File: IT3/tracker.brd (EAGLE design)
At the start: 120 x 89.3 mm, 91 parts, among them J1 THING_PLUS_PHYSICAL, Q1 2N3906, Q2 DMG6602SVT, Q3 DMG6602SVT, Q6 MMBT3906LT1SMD, Q7 DMG6602SVT, U1 ADXL343BCCZ-RL7, U2 FONA-800-BREAKOUTNOHOLE, U3 MP2155GQ-Z, U4 SPARKFUN-SWARM-M138NOTOPHOLE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

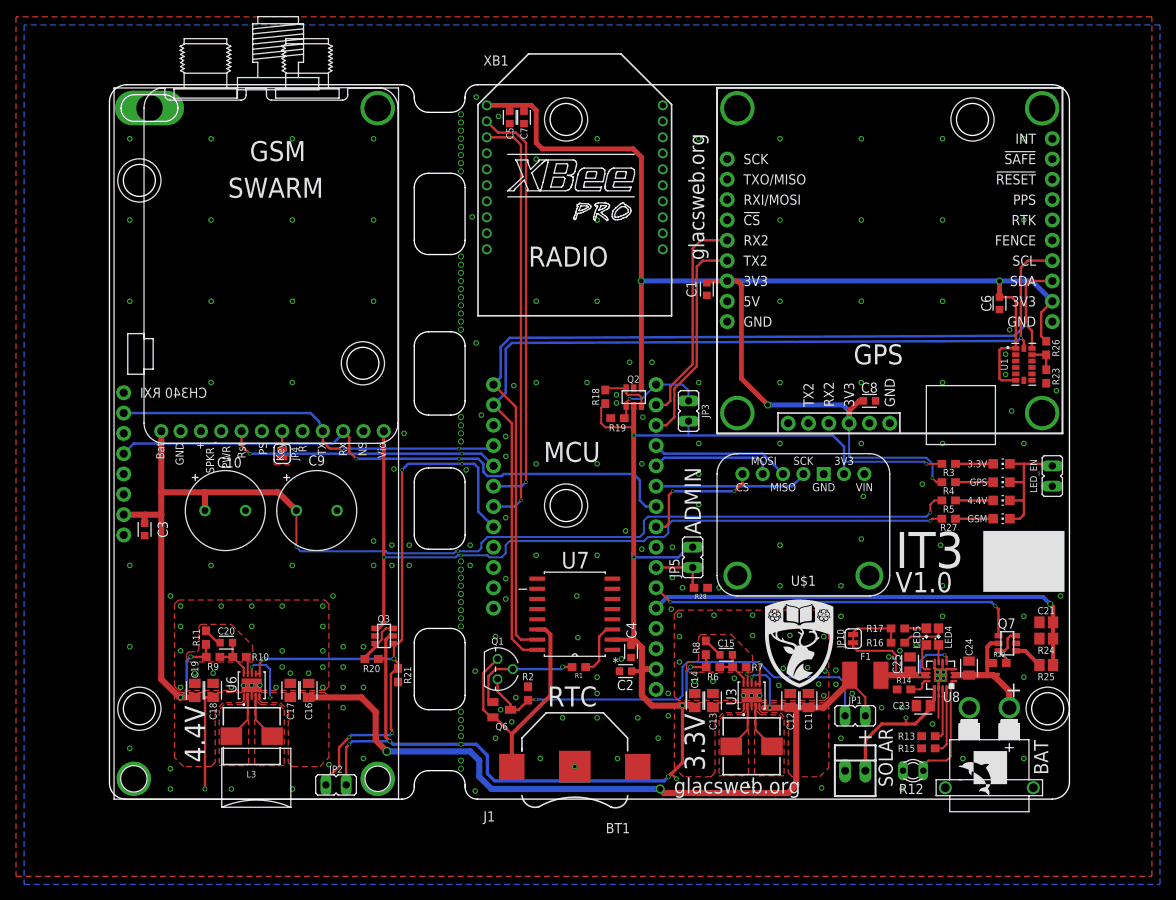
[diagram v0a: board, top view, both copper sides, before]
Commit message: Final silkscreen tweaks and generation of production files
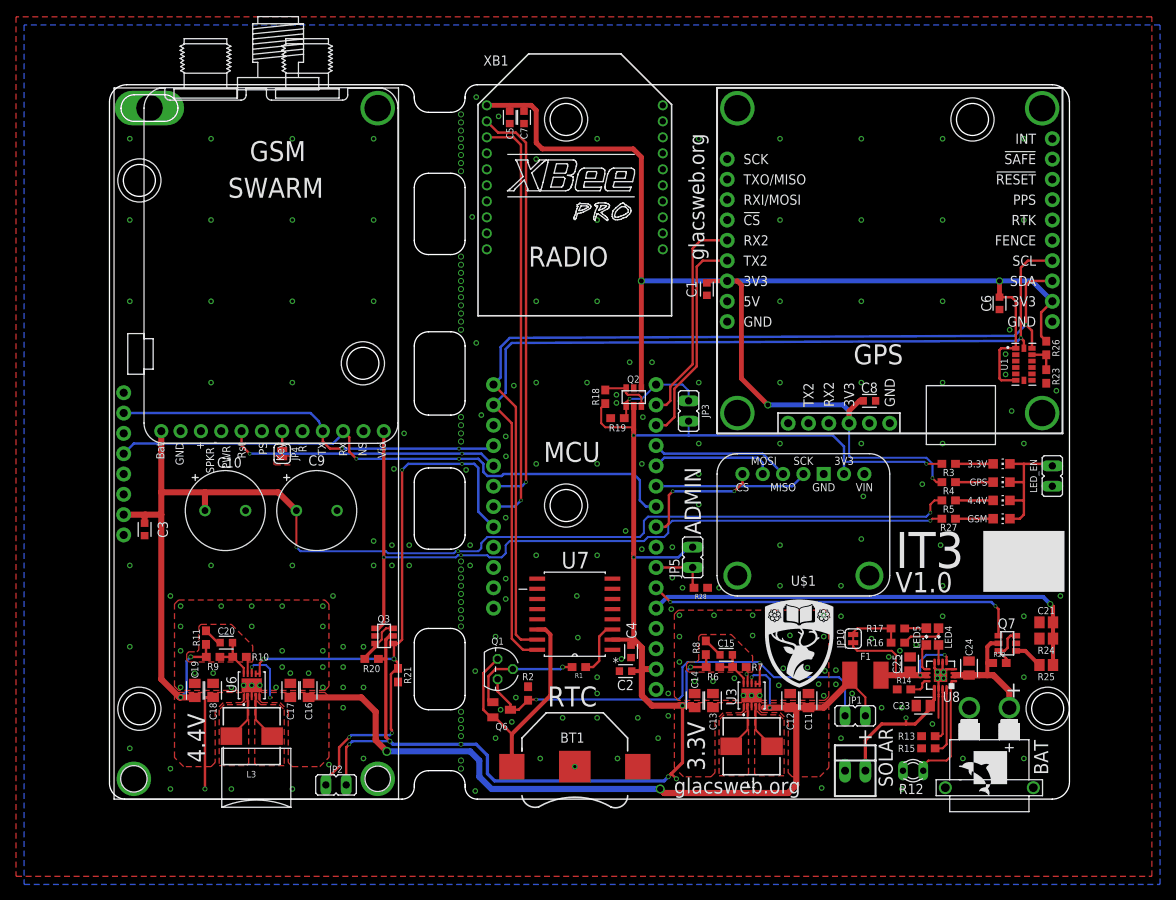
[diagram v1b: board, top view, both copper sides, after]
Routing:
- net V_BATT: track 16.9 -> 16.3 mm
- net GND: vias 242 -> 243
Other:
- board text added: "If you can read this, I am broken. Please visit: http://glacsweb.org or mail km@ecs.soton.ac.uk"
- board text removed: "If you can read this, I am broken. Please visit: http://glacsweb.org"
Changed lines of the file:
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@@
 <grid distance="10" unitdist="mil" unit="mil" style="lines" multiple="1" display="yes" altdistance="5" altunitdist="mil" altunit="mil"/>
 <layers>
-<layer number="1" name="Top" color="4" fill="1" visible="no" active="yes"/>
+<layer number="1" name="Top" color="4" fill="1" visible="yes" active="yes"/>
 <layer number="2" name="Route2" color="16" fill="1" visible="no" active="no"/>
 <layer number="3" name="Route3" color="17" fill="1" visible="no" active="no"/>
@@
 <layer number="19" name="Unrouted" color="6" fill="1" visible="yes" active="yes"/>
 <layer number="20" name="Dimension" color="24" fill="1" visible="yes" active="yes"/>
-<layer number="21" name="tPlace" color="7" fill="1" visible="no" active="yes"/>
-<layer number="22" name="bPlace" color="7" fill="1" visible="yes" active="yes"/>
-<layer number="23" name="tOrigins" color="15" fill="1" visible="no" active="yes"/>
-<layer number="24" name="bOrigins" color="15" fill="1" visible="yes" active="yes"/>
-<layer number="25" name="tNames" color="7" fill="1" visible="no" active="yes"/>
-<layer number="26" name="bNames" color="7" fill="1" visible="yes" active="yes"/>
+<layer number="21" name="tPlace" color="7" fill="1" visible="yes" active="yes"/>
+<layer number="22" name="bPlace" color="7" fill="1" visible="no" active="yes"/>
+<layer number="23" name="tOrigins" color="15" fill="1" visible="yes" active="yes"/>
+<layer number="24" name="bOrigins" color="15" fill="1" visible="no" active="yes"/>
+<layer number="25" name="tNames" color="7" fill="1" visible="yes" active="yes"/>
+<layer number="26" name="bNames" color="7" fill="1" visible="no" active="yes"/>
 <layer number="27" name="tValues" color="7" fill="1" visible="no" active="yes"/>
 <layer number="28" name="bValues" color="7" fill="1" visible="no" active="yes"/>
@@
 <text x="94.488" y="6.858" size="2.032" layer="25" align="bottom-center">+</text>
 <text x="113.03" y="12.7" size="2.032" layer="25" align="bottom-center">+</text>
-<text x="74.422" y="3.556" size="2.54" layer="21" ratio="15" rot="R90">3.3V</text>
-<text x="11.938" y="4.572" size="2.54" layer="21" ratio="15" rot="R90">4.4V</text>
+<text x="74.422" y="3.556" size="2.1844" layer="21" ratio="15" rot="R90">3.3V</text>
+<text x="11.938" y="4.572" size="2.1844" layer="21" ratio="15" rot="R90">4.4V</text>
 <wire x1="44.45" y1="87.776" x2="44.45" y2="87.63" width="0" layer="20"/>
 <wire x1="44.45" y1="76.454" x2="44.45" y2="69.85" width="0" layer="20"/>
@@
 <text x="98.242" y="28.896" size="4.5" layer="25" font="vector" ratio="15">IT3</text>
 <text x="98.242" y="25.848" size="2.54" layer="25" font="vector" ratio="15">V1.0</text>
-<text x="120.221" y="37.388" size="2.1844" layer="22" font="fixed" rot="MR270">Graeme Bragg
+<text x="119.459" y="37.388" size="2.1844" layer="22" font="fixed" rot="MR270">Graeme Bragg
 Kirk Martinez
 Sherif Attia
@@
 <text x="70.556" y="0.702" size="1.9304" layer="25" font="vector" ratio="15">glacsweb.org</text>
 <text x="74.355" y="67.381" size="1.9304" layer="25" font="vector" ratio="15" rot="R90">glacsweb.org</text>
-<text x="82.217" y="1.982" size="2.1844" layer="22" font="fixed" rot="MR90">I am a piece of
+<text x="77.391" y="2.236" size="2.1844" layer="22" font="fixed" rot="MR90">I am a piece of
 scientific equipment
-for glacier monitoring.</text>
-<text x="51.483" y="0.712" size="2.1844" layer="22" font="fixed" rot="MR90">If you can read this,
+for glacier
+monitoring.</text>
+<text x="51.483" y="1.22" size="2.1844" layer="22" font="fixed" rot="MR90">If you can read this,
 I am broken.
 Please visit:
-http://glacsweb.org</text>
+http://glacsweb.org
+or mail km@ecs.soton.ac.uk</text>
 </plain>
 <attributes>
@@
 </class>
 </classes>
-<designrules name="jlcpcb2layer">
+<designrules name="jlcpcb2layer *">
 <description language="en">&lt;b&gt;JLCPCB Design Rules by Jaap de Dood&lt;/b&gt;
 &lt;p&gt;
@@
 <param name="mlMinCreamFrame" value="0mil"/>
 <param name="mlMaxCreamFrame" value="0mil"/>
-<param name="mlViaStopLimit" value="0mil"/>
+<param name="mlViaStopLimit" value="20mil"/>
 <param name="srRoundness" value="0"/>
 <param name="srMinRoundness" value="0mil"/>
@@
 <element name="U5" library="GlacTracker" package="SPARKFUN-GPS-ZED-F9P" value="SPARKFUN-GPS-ZED-F9P" x="119.126" y="45.72" smashed="yes" rot="R90"/>
 <element name="J1" library="SparkFun-Boards" package="THING_PLUS" value="THING_PLUS_PHYSICAL" x="46.736" y="-0.254" smashed="yes">
-<attribute name="NAME" x="46.736" y="-2.794" size="1.27" layer="25" font="vector"/>
 <attribute name="VALUE" x="46.736" y="59.436" size="1.27" layer="27" font="vector"/>
 </element>
@@
 <attribute name="MF" value="Keystone" x="58.166" y="4.064" size="1.778" layer="27" rot="R180" display="off"/>
 <attribute name="MP" value="3000TR" x="58.166" y="4.064" size="1.778" layer="27" rot="R180" display="off"/>
-<attribute name="NAME" x="65.07118125" y="-2.991290625" size="1.27095" layer="25" rot="R180"/>
+<attribute name="NAME" x="56.34081875" y="7.055290625" size="1.27095" layer="25"/>
 <attribute name="PACKAGE" value="None" x="58.166" y="4.064" size="1.778" layer="27" rot="R180" display="off"/>
 <attribute name="PRICE" value="None" x="58.166" y="4.064" size="1.778" layer="27" rot="R180" display="off"/>
@@
 <via x="70.358" y="27.686" extent="1-16" drill="0.4064" diameter="0.7112"/>
 <via x="70.358" y="31.496" extent="1-16" drill="0.4064" diameter="0.7112"/>
+<via x="95.25" y="20.066" extent="1-16" drill="0.4064" diameter="0.7112"/>
 </signal>
 <signal name="GPS_RX2">
@@
 <wire x1="47.625" y1="43.815" x2="43.688" y2="43.815" width="0.3048" layer="16"/>
 <wire x1="43.688" y1="43.815" x2="29.083" y2="43.815" width="0.3048" layer="16"/>
-<wire x1="28.829" y1="43.815" x2="29.083" y2="43.815" width="0.3048" layer="1"/>
 <wire x1="26.67" y1="45.974" x2="26.67" y2="44.704" width="0.3048" layer="1"/>
 <wire x1="26.67" y1="44.704" x2="27.559" y2="43.815" width="0.3048" layer="1"/>
@@
 <contactref element="Q7" pad="P$2"/>
 <contactref element="R22" pad="1"/>
-<wire x1="111.078" y1="15.574" x2="110.49" y2="15.494" width="0.508" layer="1"/>
 <wire x1="111.13" y1="19.478" x2="110.156" y2="19.478" width="0.508" layer="1"/>
 <wire x1="110.156" y1="19.478" x2="109.728" y2="19.05" width="0.508" layer="1"/>
